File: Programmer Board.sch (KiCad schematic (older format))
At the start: 0 parts

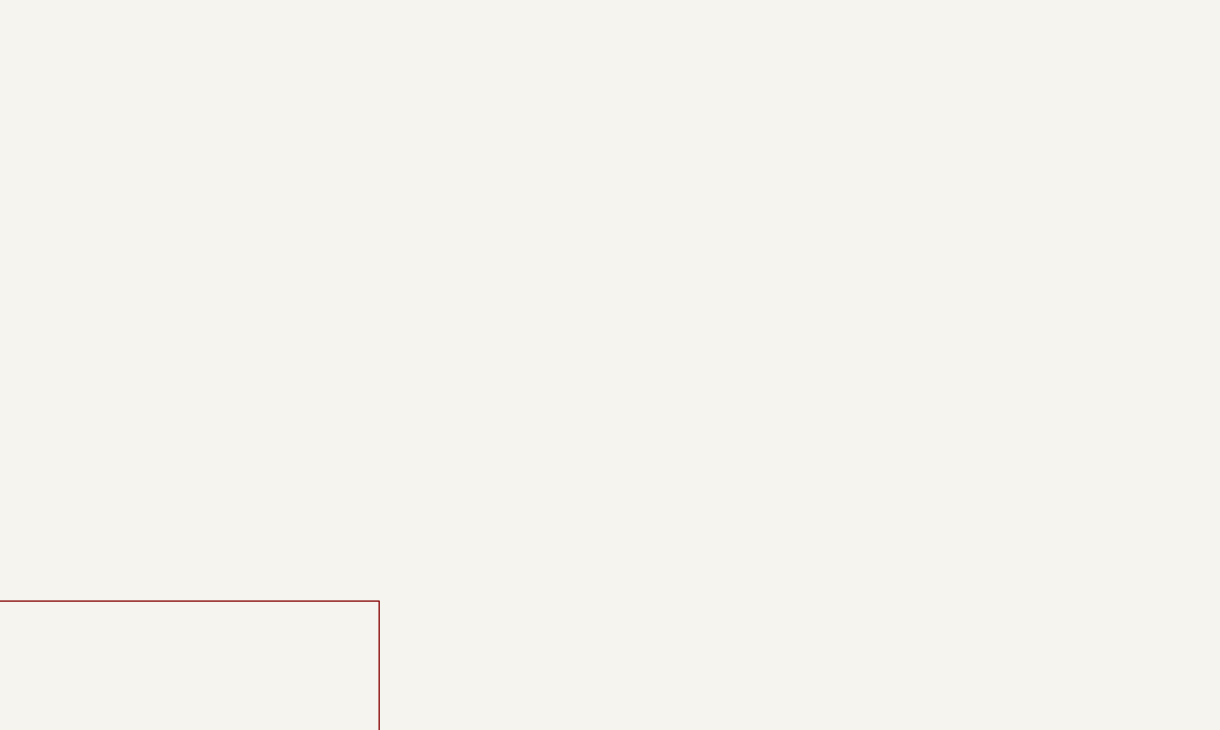
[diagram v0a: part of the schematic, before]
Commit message: Added DC-DC converter
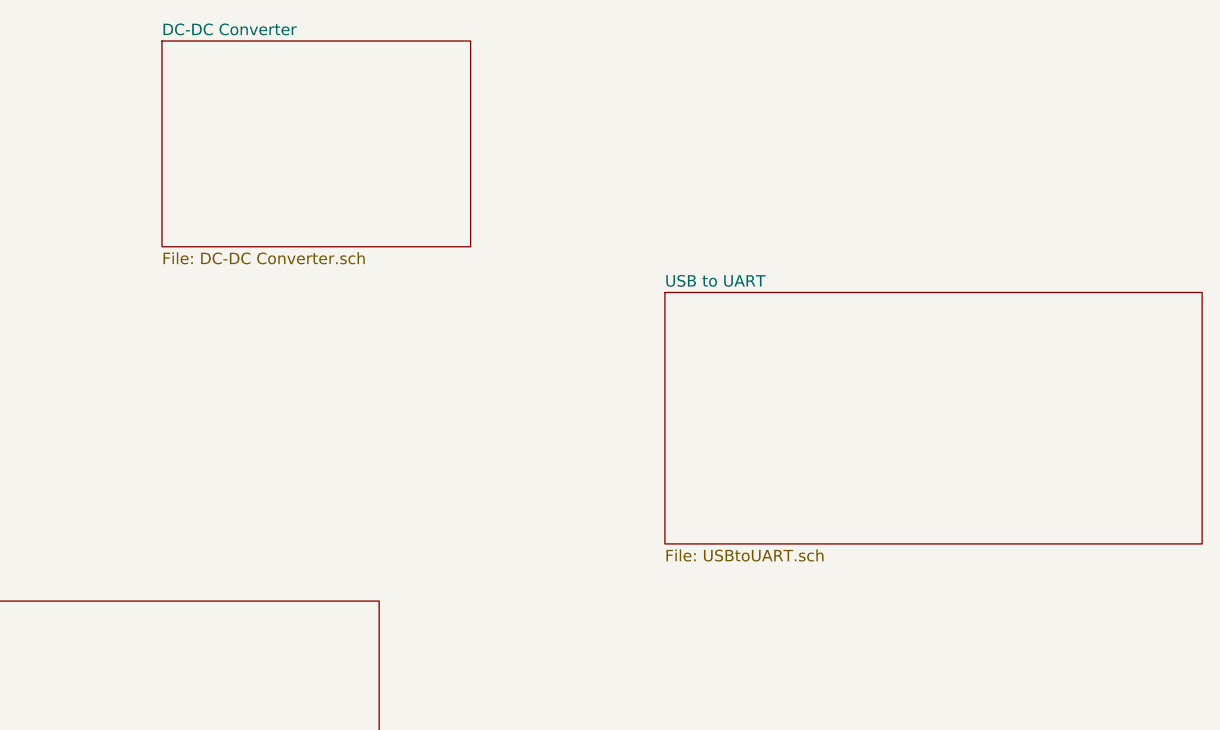
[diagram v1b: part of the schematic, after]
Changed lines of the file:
@@
 $Descr A4 11693 8268
 encoding utf-8
-Sheet 1 2
+Sheet 1 4
 Title ""
 Date ""
@@
 F3 "ST7-ICCDATA" I L 2800 5800 50
 $EndSheet
+$Sheet
+S 6800 3200 2350 1100
+U 5F8460BD
+F0 "USB to UART" 50
+F1 "USBtoUART.sch" 50
+$EndSheet
+$Sheet
+S 4600 2100 1350 900
+U 5F8D08F6
+F0 "DC-DC Converter" 50
+F1 "DC-DC Converter.sch" 50
+$EndSheet
 $EndSCHEMATC

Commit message: Added libraries used in the project. Top level connections.
Added libraries used in this project to the project folder.

Made additonal top level connections on the top level schematic.
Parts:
- added J?: Conn_01x03, symbol Connector_Generic:Conn_01x03
- added J?: 105-1103-001, digikey-footprints:Test_Jack_Horiz, symbol dk_Banana-and-Tip-Connectors-Jacks-Plugs:105-1103-001
- added J?: 105-1102-001, digikey-footprints:Test_Jack_Horiz, symbol dk_Banana-and-Tip-Connectors-Jacks-Plugs:105-1102-001
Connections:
- new net: J?.1, J?.1 (Pin_1)
- new net DC-DC Converter/+V_in: J?.2 (Pin_2)
- new net GND: J?.1
- new net USB to UART/+5_USB: J?.3 (Pin_3)
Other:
- note added: "External power source select. \nJumper 1-2 for banana jacks. \nJumper 2-3 for USB power."
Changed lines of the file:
@@
 $EndDescr
 $Sheet
-S 2800 4550 2750 1700
+S 7350 1300 2700 2750
 U 5F7C6408
 F0 "Card Edge Conn" 50
 F1 "CardEdgeConn.sch" 50
-F2 "ST7-ICCSEL" I L 2800 6000 50
-F3 "ST7-ICCDATA" I L 2800 5800 50
+F2 "ST7-ICCSEL" I L 7350 2750 50
+F3 "ST7-ICCDATA" I L 7350 2550 50
+F4 "U21.20-DCLK" I L 7350 1550 50
+F5 "SW1.1" I L 7350 1700 50
+F6 "GPS.?D" I L 7350 1800 50
+F7 "U22.3" I L 7350 1900 50
+F8 "J5.3" I L 7350 2000 50
+F9 "SW1.3" I L 7350 2100 50
+F10 "U3.18" I L 7350 2200 50
+F11 "GPS.??D" I L 7350 2300 50
+F12 "U3.19" I L 7350 2400 50
+F13 "SW1.2" I R 10050 1600 50
+F14 "SW1.4" I R 10050 1700 50
+F15 "J5.2" I R 10050 1800 50
+F16 "ST7-RESET" I R 10050 2000 50
+F17 "ST7-ICCCLK" I R 10050 2100 50
+F18 "HEADER1.1" I R 10050 2200 50
+F19 "HEADER1.2" I R 10050 2300 50
+F20 "HEADER1.3" I R 10050 2400 50
+F21 "HEADER1.4" I R 10050 2500 50
+F22 "HEADER1.5" I R 10050 2600 50
+F23 "HEADER1.6" I R 10050 2700 50
+F24 "HEADER1.7" I R 10050 2800 50
+F25 "HEADER1.9" I R 10050 2900 50
+F26 "HEADER1.10" I R 10050 3000 50
+F27 "9V_PS" I L 7350 1350 50
 $EndSheet
 $Sheet
-S 6800 3200 2350 1100
+S 3250 2300 1050 650
 U 5F8460BD
 F0 "USB to UART" 50
 F1 "USBtoUART.sch" 50
+F2 "+5_USB" I L 3250 2500 50
+F3 "GPS.TXD" I R 4300 2500 50
+F4 "GPS.RXD" I R 4300 2600 50
+F5 "UART2.RXD" I R 4300 2700 50
+F6 "UART2.TXD" I R 4300 2800 50
 $EndSheet
 $Sheet
-S 4600 2100 1350 900
+S 5400 1150 950  450
 U 5F8D08F6
 F0 "DC-DC Converter" 50
 F1 "DC-DC Converter.sch" 50
+F2 "+V_in" I L 5400 1350 50
+F3 "+V_out" I R 6350 1350 50
 $EndSheet
+$Comp
+L Connector_Generic:Conn_01x03 J?
+U 1 1 5F8A4B7F
+P 2550 1350
+AR Path="/5F7C6408/5F8A4B7F" Ref="J?"  Part="1"
+AR Path="/5F8A4B7F" Ref="J?"  Part="1"
+F 0 "J?" H 2468 1667 50  0000 C CNN
+F 1 "Conn_01x03" H 2468 1576 50  0000 C CNN
+F 2 "" H 2550 1350 50  0001 C CNN
+F 3 "~" H 2550 1350 50  0001 C CNN
+	1    2550 1350
+	-1   0    0    -1
+$EndComp
+Wire Wire Line
+	1500 1300 1500 1200
+$Comp
+L power:GND #PWR?
+U 1 1 5F8A4B86
+P 1500 1300
+AR Path="/5F8D08F6/5F8A4B86" Ref="#PWR?"  Part="1"
+AR Path="/5F8A4B86" Ref="#PWR?"  Part="1"
+F 0 "#PWR?" H 1500 1050 50  0001 C CNN
+F 1 "GND" H 1505 1127 50  0000 C CNN
+F 2 "" H 1500 1300 50  0001 C CNN
+F 3 "" H 1500 1300 50  0001 C CNN
+	1    1500 1300
+	1    0    0    -1
+$EndComp
+$Comp
+L dk_Banana-and-Tip-Connectors-Jacks-Plugs:105-1103-001 J?
+U 1 1 5F8A4B95
+P 1500 1050
+AR Path="/5F8D08F6/5F8A4B95" Ref="J?"  Part="1"
+AR Path="/5F8A4B95" Ref="J?"  Part="1"
+F 0 "J?" H 1578 1038 50  0000 L CNN
+F 1 "105-1103-001" H 1578 947 50  0000 L CNN
+F 2 "digikey-footprints:Test_Jack_Horiz" H 1700 1250 60  0001 L CNN
+F 3 "https://belfuse.com/resources/Johnson/drawings/dr-1051101001.pdf" H 1700 1350 60  0001 L CNN
+F 4 "J577-ND" H 1700 1450 60  0001 L CNN "Digi-Key_PN"
+F 5 "105-1103-001" H 1700 1550 60  0001 L CNN "MPN"
+F 6 "Connectors, Interconnects" H 1700 1650 60  0001 L CNN "Category"
+F 7 "Banana and Tip Connectors - Jacks, Plugs" H 1700 1750 60  0001 L CNN "Family"
+F 8 "https://belfuse.com/resources/Johnson/drawings/dr-1051101001.pdf" H 1700 1850 60  0001 L CNN "DK_Datasheet_Link"
+F 9 "/product-detail/en/cinch-connectivity-solutions-johnson/105-1103-001/J577-ND/241122" H 1700 1950 60  0001 L CNN "DK_Detail_Page"
+F 10 "CONN TIP JACK SOLDER BLACK" H 1700 2050 60  0001 L CNN "Description"
+F 11 "Cinch Connectivity Solutions Johnson" H 1700 2150 60  0001 L CNN "Manufacturer"
+F 12 "Active" H 1700 2250 60  0001 L CNN "Status"
+	1    1500 1050
+	1    0    0    -1
+$EndComp
+$Comp
+L dk_Banana-and-Tip-Connectors-Jacks-Plugs:105-1102-001 J?
+U 1 1 5F8A4BA4
+P 3200 1050
+AR Path="/5F8D08F6/5F8A4BA4" Ref="J?"  Part="1"
+AR Path="/5F8A4BA4" Ref="J?"  Part="1"
+F 0 "J?" H 3278 1038 50  0000 L CNN
+F 1 "105-1102-001" H 3278 947 50  0000 L CNN
+F 2 "digikey-footprints:Test_Jack_Horiz" H 3400 1250 60  0001 L CNN
+F 3 "https://belfuse.com/resources/Johnson/drawings/dr-1051101001.pdf" H 3400 1350 60  0001 L CNN
+F 4 "J576-ND" H 3400 1450 60  0001 L CNN "Digi-Key_PN"
+F 5 "105-1102-001" H 3400 1550 60  0001 L CNN "MPN"
+F 6 "Connectors, Interconnects" H 3400 1650 60  0001 L CNN "Category"
+F 7 "Banana and Tip Connectors - Jacks, Plugs" H 3400 1750 60  0001 L CNN "Family"
+F 8 "https://belfuse.com/resources/Johnson/drawings/dr-1051101001.pdf" H 3400 1850 60  0001 L CNN "DK_Datasheet_Link"
+F 9 "/product-detail/en/cinch-connectivity-solutions-johnson/105-1102-001/J576-ND/241121" H 3400 1950 60  0001 L CNN "DK_Detail_Page"
+F 10 "CONN TIP JACK SOLDER RED" H 3400 2050 60  0001 L CNN "Description"
+F 11 "Cinch Connectivity Solutions Johnson" H 3400 2150 60  0001 L CNN "Manufacturer"
+F 12 "Active" H 3400 2250 60  0001 L CNN "Status"
+	1    3200 1050
+	1    0    0    -1
+$EndComp
+Wire Wire Line
+	2750 1250 3200 1250
+Wire Wire Line
+	3200 1250 3200 1200
+Wire Wire Line
+	2750 1350 5400 1350
+Text Notes 2000 850  0    50   ~ 0
+External power source select. \nJumper 1-2 for banana jacks. \nJumper 2-3 for USB power.
+Wire Wire Line
+	3250 2500 2950 2500
+Wire Wire Line
+	2950 2500 2950 1450
+Wire Wire Line
+	2950 1450 2750 1450
+Wire Wire Line
+	6350 1350 7350 1350
 $EndSCHEMATC

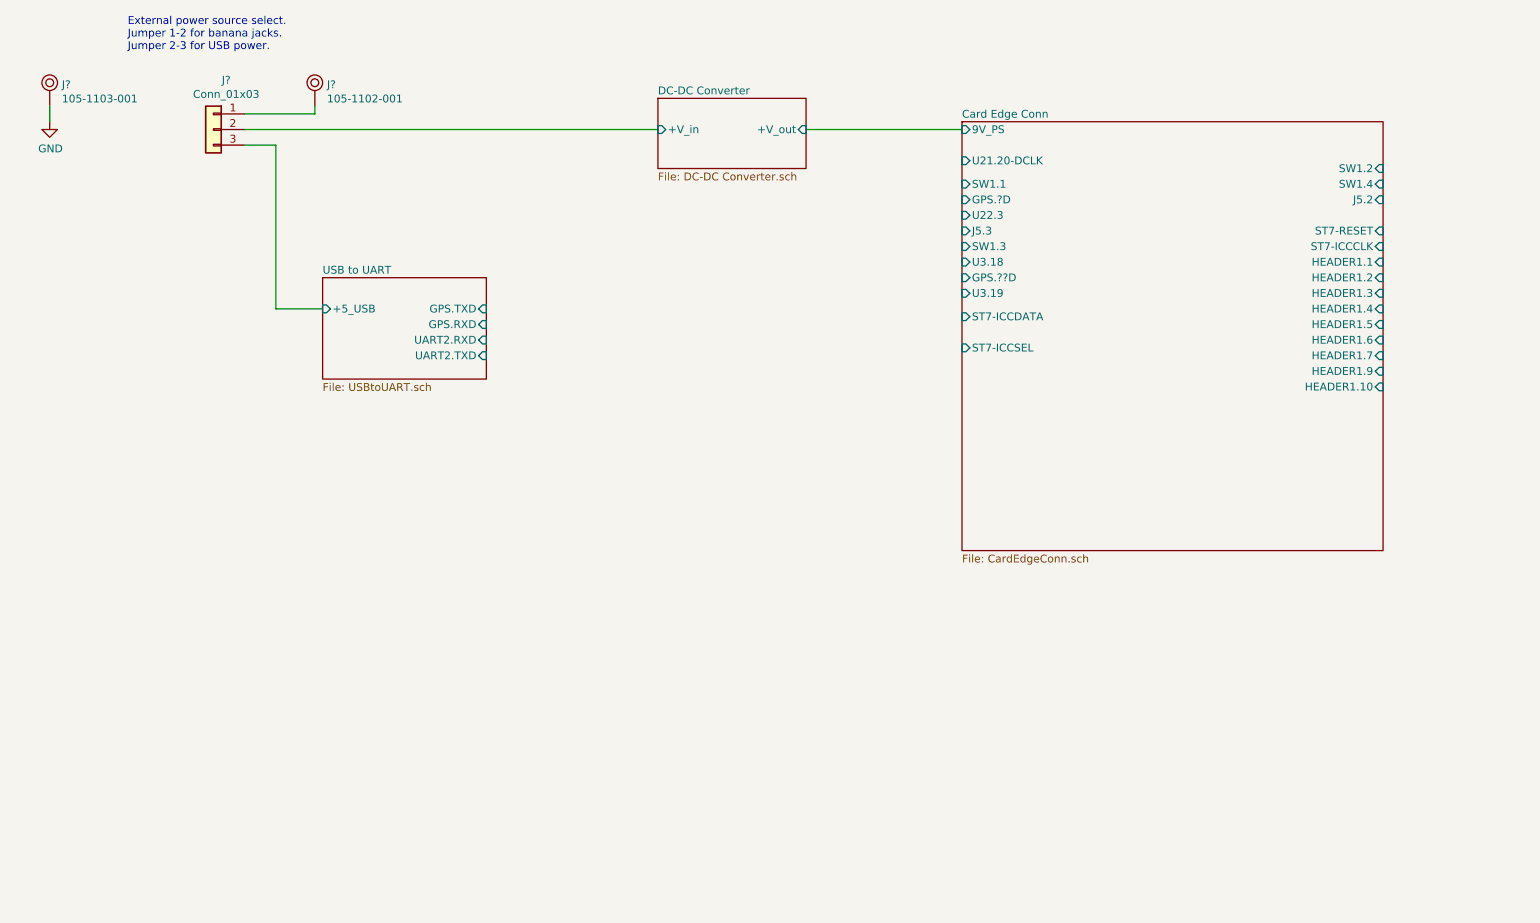
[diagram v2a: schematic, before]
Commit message: Annotated schematics and added UART Jumpers
Annotated schematics.

Added jumpers to GPS UART because I'm still not 100% sure on the connections and I don't want to have to respin a board because I was wrong.
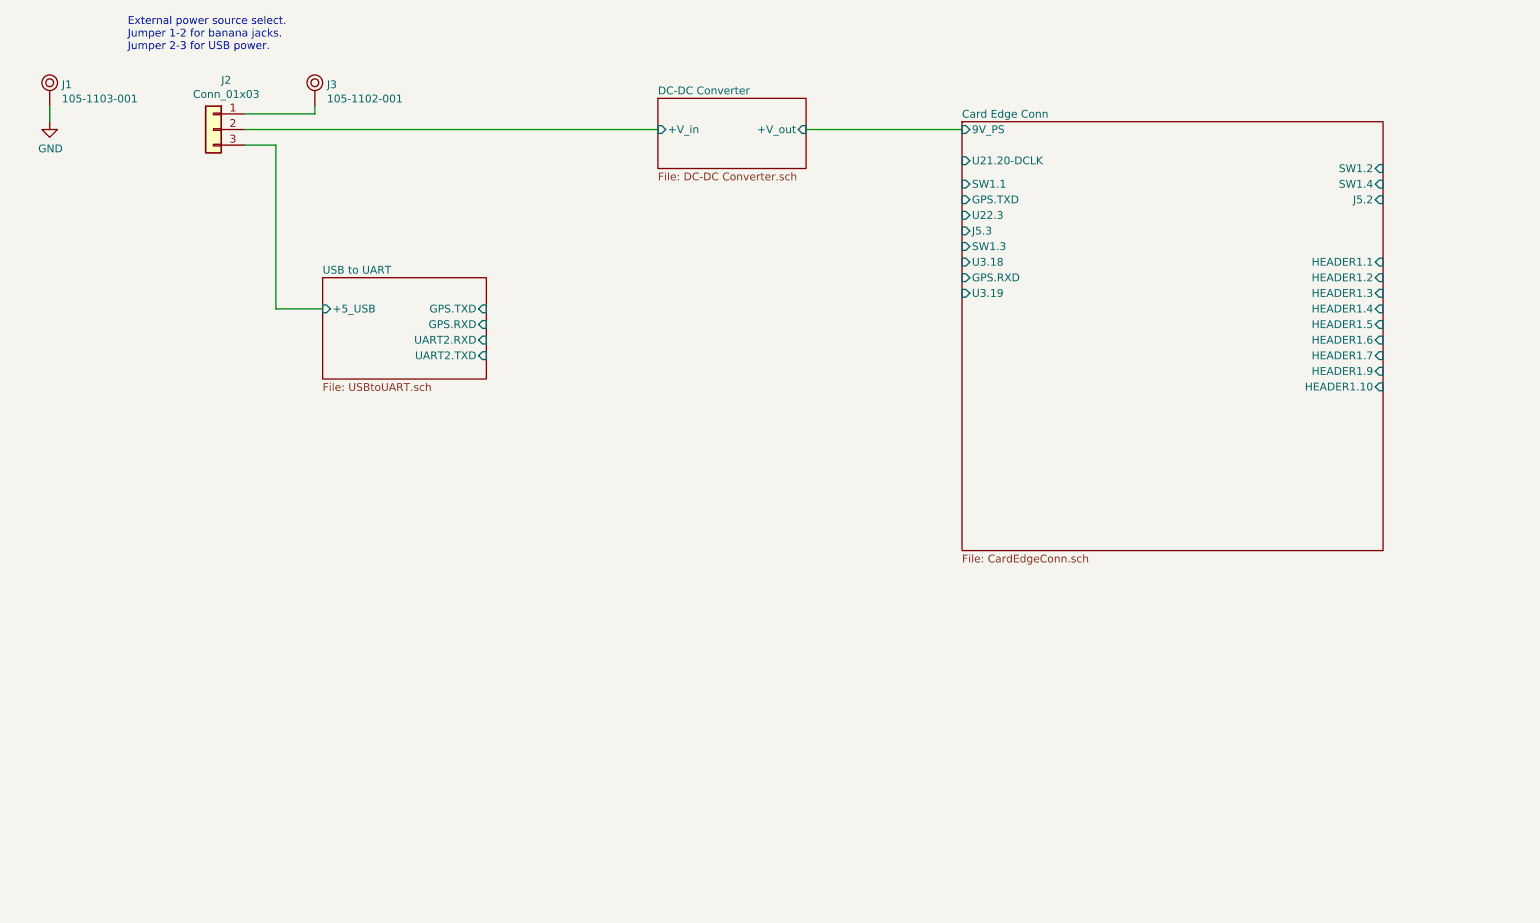
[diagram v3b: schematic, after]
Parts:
- gave numbers to parts that had none: 3
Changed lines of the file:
@@
 $EndDescr
-$Sheet
-S 7350 1300 2700 2750
-U 5F7C6408
-F0 "Card Edge Conn" 50
-F1 "CardEdgeConn.sch" 50
-F2 "ST7-ICCSEL" I L 7350 2750 50
-F3 "ST7-ICCDATA" I L 7350 2550 50
-F4 "U21.20-DCLK" I L 7350 1550 50
-F5 "SW1.1" I L 7350 1700 50
-F6 "GPS.?D" I L 7350 1800 50
-F7 "U22.3" I L 7350 1900 50
-F8 "J5.3" I L 7350 2000 50
-F9 "SW1.3" I L 7350 2100 50
-F10 "U3.18" I L 7350 2200 50
-F11 "GPS.??D" I L 7350 2300 50
-F12 "U3.19" I L 7350 2400 50
-F13 "SW1.2" I R 10050 1600 50
-F14 "SW1.4" I R 10050 1700 50
-F15 "J5.2" I R 10050 1800 50
-F16 "ST7-RESET" I R 10050 2000 50
-F17 "ST7-ICCCLK" I R 10050 2100 50
-F18 "HEADER1.1" I R 10050 2200 50
-F19 "HEADER1.2" I R 10050 2300 50
-F20 "HEADER1.3" I R 10050 2400 50
-F21 "HEADER1.4" I R 10050 2500 50
-F22 "HEADER1.5" I R 10050 2600 50
-F23 "HEADER1.6" I R 10050 2700 50
-F24 "HEADER1.7" I R 10050 2800 50
-F25 "HEADER1.9" I R 10050 2900 50
-F26 "HEADER1.10" I R 10050 3000 50
-F27 "9V_PS" I L 7350 1350 50
-$EndSheet
 $Sheet
 S 3250 2300 1050 650
@@
 P 2550 1350
 AR Path="/5F7C6408/5F8A4B7F" Ref="J?"  Part="1"
-AR Path="/5F8A4B7F" Ref="J?"  Part="1"
-F 0 "J?" H 2468 1667 50  0000 C CNN
+AR Path="/5F8A4B7F" Ref="J2"  Part="1"
+F 0 "J2" H 2468 1667 50  0000 C CNN
 F 1 "Conn_01x03" H 2468 1576 50  0000 C CNN
 F 2 "" H 2550 1350 50  0001 C CNN
@@
 P 1500 1300
 AR Path="/5F8D08F6/5F8A4B86" Ref="#PWR?"  Part="1"
-AR Path="/5F8A4B86" Ref="#PWR?"  Part="1"
-F 0 "#PWR?" H 1500 1050 50  0001 C CNN
+AR Path="/5F8A4B86" Ref="#PWR01"  Part="1"
+F 0 "#PWR01" H 1500 1050 50  0001 C CNN
 F 1 "GND" H 1505 1127 50  0000 C CNN
 F 2 "" H 1500 1300 50  0001 C CNN
@@
 P 1500 1050
 AR Path="/5F8D08F6/5F8A4B95" Ref="J?"  Part="1"
-AR Path="/5F8A4B95" Ref="J?"  Part="1"
-F 0 "J?" H 1578 1038 50  0000 L CNN
+AR Path="/5F8A4B95" Ref="J1"  Part="1"
+F 0 "J1" H 1578 1038 50  0000 L CNN
 F 1 "105-1103-001" H 1578 947 50  0000 L CNN
 F 2 "digikey-footprints:Test_Jack_Horiz" H 1700 1250 60  0001 L CNN
@@
 P 3200 1050
 AR Path="/5F8D08F6/5F8A4BA4" Ref="J?"  Part="1"
-AR Path="/5F8A4BA4" Ref="J?"  Part="1"
-F 0 "J?" H 3278 1038 50  0000 L CNN
+AR Path="/5F8A4BA4" Ref="J3"  Part="1"
+F 0 "J3" H 3278 1038 50  0000 L CNN
 F 1 "105-1102-001" H 3278 947 50  0000 L CNN
 F 2 "digikey-footprints:Test_Jack_Horiz" H 3400 1250 60  0001 L CNN
@@
 Wire Wire Line
 	6350 1350 7350 1350
+$Sheet
+S 7350 1300 2700 2750
+U 5F7C6408
+F0 "Card Edge Conn" 50
+F1 "CardEdgeConn.sch" 50
+F2 "U21.20-DCLK" I L 7350 1550 50
+F3 "SW1.1" I L 7350 1700 50
+F4 "GPS.TXD" I L 7350 1800 50
+F5 "U22.3" I L 7350 1900 50
+F6 "J5.3" I L 7350 2000 50
+F7 "SW1.3" I L 7350 2100 50
+F8 "U3.18" I L 7350 2200 50
+F9 "GPS.RXD" I L 7350 2300 50
+F10 "U3.19" I L 7350 2400 50
+F11 "SW1.2" I R 10050 1600 50
+F12 "SW1.4" I R 10050 1700 50
+F13 "J5.2" I R 10050 1800 50
+F14 "HEADER1.1" I R 10050 2200 50
+F15 "HEADER1.2" I R 10050 2300 50
+F16 "HEADER1.3" I R 10050 2400 50
+F17 "HEADER1.4" I R 10050 2500 50
+F18 "HEADER1.5" I R 10050 2600 50
+F19 "HEADER1.6" I R 10050 2700 50
+F20 "HEADER1.7" I R 10050 2800 50
+F21 "HEADER1.9" I R 10050 2900 50
+F22 "HEADER1.10" I R 10050 3000 50
+F23 "9V_PS" I L 7350 1350 50
+$EndSheet
 $EndSCHEMATC
